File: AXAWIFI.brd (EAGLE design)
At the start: 94 x 27.9 mm, 24 parts, among them IC1 MCP2003, IC2 ESP12SMT, M1 REGMODULE4PIN, SW1 RESET, SW2 REFLASH

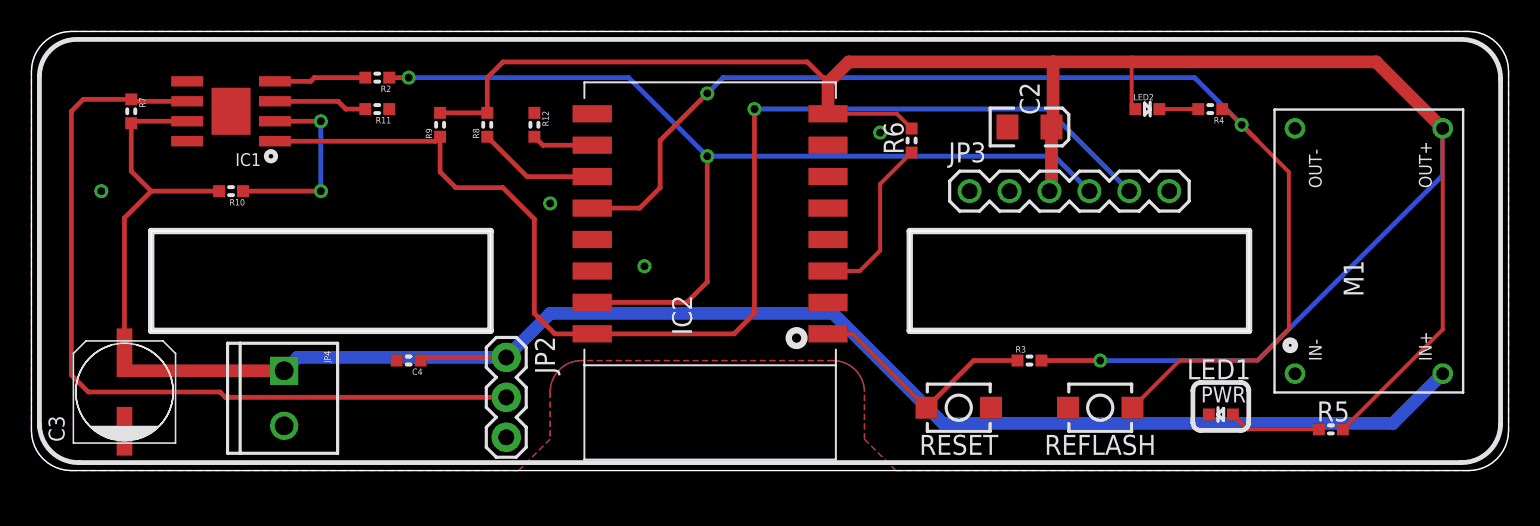
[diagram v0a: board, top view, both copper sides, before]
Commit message: Replaced voltage regulator module with K7833 for v1.1 release
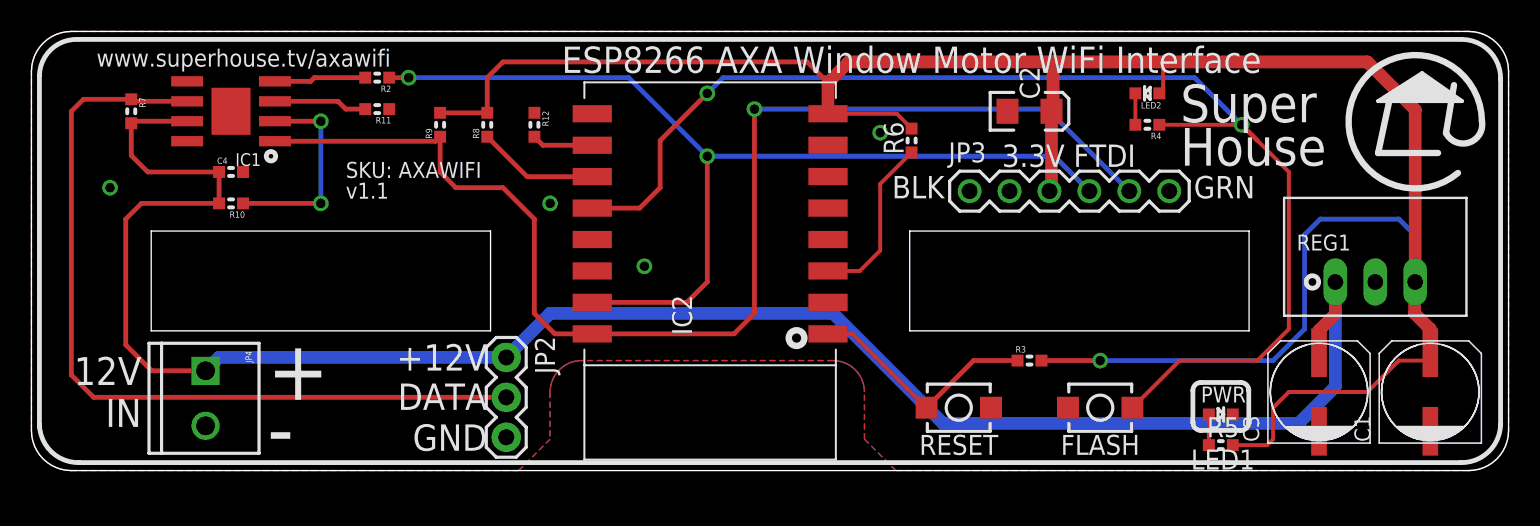
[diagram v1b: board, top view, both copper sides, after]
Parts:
- removed M1: REGMODULE4PIN, freetronics-jon:REGMODULE4PIN
- added C1: 22uF 40V, analyzer:UD-6,3X5,8_NICHICON
- added REG1: K7833-500R3, freetronics-jon:K78XX-500R3
- moved C3 76.0 mm to (81.9, 5.00)
- moved C4 16.5 mm to (12.7, 19.0), turned to 0 degrees
- moved R5 7.07 mm to (75.7, 1.62)
- moved JP4 5.00 mm to (11.1, 6.35)
- moved R4 4.12 mm to (71.0, 22.0)
- moved C2 1.00 mm to (63.5, 22.9)
- moved LED2 1.00 mm to (71.0, 24.0), turned to 180 degrees
- moved R10 0.78 mm to (12.7, 17.0)
- turned LED1 to 0 degrees
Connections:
- net +12V: now also REG1.1; no longer M1.2
- net 3.3V: now also C1.+, REG1.3; no longer M1.3
- net GND: now also C1.-, REG1.2; no longer M1.1, M1.4
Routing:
- net 3.3V: track 143.7 -> 152.1 mm
- net N$14: track 5.87 -> 1.95 mm
- net GPIO0: track 75.7 -> 79.3 mm
- net +12V: track 120.0 -> 122.7 mm
- net N$5: track 12.3 -> 13.1 mm
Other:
- board text added: "(c) 2018 SuperHouse Automation Pty Ltd Released under the TAPR Open Hardware License www.tapr.org/OHL"
- board text added: "+"
- board text added: "+12V"
- board text added: "-"
- board text added: "12V IN"
- board text added: "3.3V FTDI"
- board text added: "BLK"
- board text added: "CH_PD biased HIGH by default GPIO0 pulled LOW by FLASH"
- board text added: "DATA"
- board text added: "ESP8266 AXA Window Motor WiFi Interface"
- board text added: "FLASH"
- board text added: "GND"
- board text added: "GRN"
- board text added: "SKU: AXAWIFI v1.1"
- board text added: "Super House"
- board text added: "www.superhouse.tv/axawifi"
- board text removed: "(c) 2017 SuperHouse Automation Pty Ltd Released under the TAPR Open Hardware License www.tapr.org/OHL"
- board text removed: "CH_PD biased HIGH by default GPIO0 pulled LOW by REFLASH"
- board text removed: "REFLASH"
